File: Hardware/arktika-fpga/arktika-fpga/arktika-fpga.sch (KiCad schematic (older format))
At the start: 0 parts

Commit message: Misc schematic changes. Preliminary layout almost complete
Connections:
- net labels added: D+, D-, GNDPLL0, GNDPLL1
- wire segments 19 -> 25
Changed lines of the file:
@@
 F11 "VCC5V" I R 3850 3900 50
 F12 "GND" I L 2550 4050 50
+F13 "GNDPLL0" I L 2550 3950 50
+F14 "GNDPLL1" I L 2550 3850 50
 $EndSheet
 $Sheet
@@
 F10 "VBUS" I L 4350 3900 50
 F11 "GND" I R 5600 4050 50
+F12 "GNDPLL0" I R 5600 3950 50
+F13 "GNDPLL1" I R 5600 3850 50
 $EndSheet
 $Sheet
@@
 F2 "VCC3V3" I L 6300 3200 50
 F3 "VCC5V" I L 6300 3300 50
-F4 "PUSH_BTNS" I R 7550 3200 50
-F5 "SWITCHES" I R 7550 3300 50
-F6 "LEDS" I R 7550 3400 50
-F7 "ADC" I R 7550 3500 50
-F8 "UART" I R 7550 3600 50
-F9 "Vin" I L 6300 3400 50
-F10 "Buzzer" I R 7550 3700 50
-F11 "GND" I L 6300 4050 50
+F4 "Vin" I L 6300 3400 50
+F5 "Buzzer" I R 7550 3700 50
+F6 "GND" I L 6300 4050 50
+F7 "D+" I L 6300 3550 50
+F8 "D-" I L 6300 3650 50
+F9 "PSH[0..3]" I R 7550 3200 50
+F10 "SW[0..7]" I R 7550 3300 50
+F11 "LED[0..7]" I R 7550 3400 50
 $EndSheet
 $Sheet
@@
 F0 "FPGA_PERIPHS" 50
 F1 "FPGA_PERIPHS.sch" 50
-F2 "PUSH_BTNS" I L 7950 3200 50
-F3 "SWITCHES" I L 7950 3300 50
-F4 "LEDS" I L 7950 3400 50
-F5 "ADC" I L 7950 3500 50
-F6 "UART" I L 7950 3600 50
-F7 "VCC3V3" I R 9250 3200 50
-F8 "Buzzer" I L 7950 3700 50
-F9 "GND" I R 9250 4050 50
+F2 "VCC3V3" I R 9250 3200 50
+F3 "Buzzer" I L 7950 3700 50
+F4 "GND" I R 9250 4050 50
+F5 "PSH[0..3]" I L 7950 3200 50
+F6 "SW[0..7]" I L 7950 3300 50
+F7 "LED[0..7]" I L 7950 3400 50
 $EndSheet
-Wire Bus Line
-	7550 3200 7950 3200
-Wire Bus Line
-	7550 3300 7950 3300
-Wire Bus Line
-	7550 3400 7950 3400
-Wire Bus Line
-	7550 3500 7950 3500
-Wire Bus Line
-	7550 3600 7950 3600
 Wire Wire Line
 	3850 3200 4350 3200
@@
 	2250 4050 2550 4050
 $Comp
-L power:GND #PWR0101
+L arktika-fpga-rescue:GND-power #PWR0101
 U 1 1 5F2E4558
 P 2250 4050
@@
 	5600 4050 5950 4050
 $Comp
-L power:GND #PWR0102
+L arktika-fpga-rescue:GND-power #PWR0102
 U 1 1 5F2E4A9A
 P 5950 4050
@@
 	9550 4050 9250 4050
 $Comp
-L power:GND #PWR0103
+L arktika-fpga-rescue:GND-power #PWR0103
 U 1 1 5F2E5C47
 P 9550 4050
@@
 	1    0    0    -1
 $EndComp
+Text Label 4050 3700 0    50   ~ 0
+D+
+Text Label 4050 3800 0    50   ~ 0
+D-
+Text Label 6100 3550 0    50   ~ 0
+D+
+Text Label 6100 3650 0    50   ~ 0
+D-
+Wire Wire Line
+	5900 3550 6300 3550
+Wire Wire Line
+	5900 3650 6300 3650
+Text Label 6050 3850 2    50   ~ 0
+GNDPLL0
+Text Label 6050 3950 2    50   ~ 0
+GNDPLL1
+Text Label 2150 3850 0    50   ~ 0
+GNDPLL0
+Text Label 2150 3950 0    50   ~ 0
+GNDPLL1
+Wire Wire Line
+	2150 3850 2550 3850
+Wire Wire Line
+	2550 3950 2150 3950
+Wire Wire Line
+	5600 3850 6050 3850
+Wire Wire Line
+	6050 3950 5600 3950
+Wire Bus Line
+	7550 3400 7950 3400
+Wire Bus Line
+	7550 3200 7950 3200
+Wire Bus Line
+	7950 3300 7550 3300
 $EndSCHEMATC

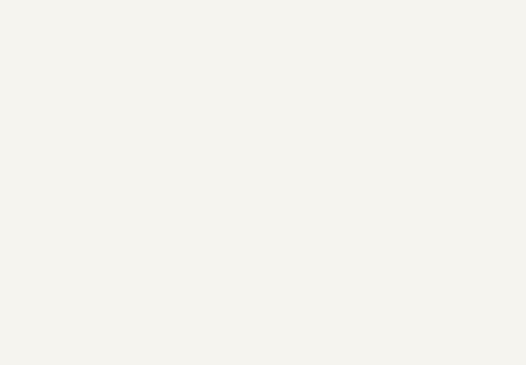
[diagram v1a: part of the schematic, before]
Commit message: Added silkscreen art and added media folder with the same art
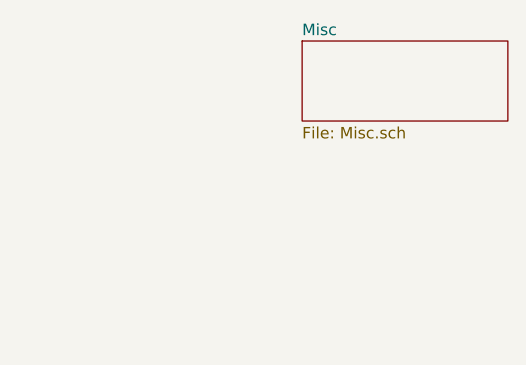
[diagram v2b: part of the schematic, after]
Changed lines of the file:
@@
 $Descr A4 11693 8268
 encoding utf-8
-Sheet 1 5
+Sheet 1 6
 Title "Arktika FPGA"
 Date "2020-07-30"
@@
 Wire Bus Line
 	7950 3300 7550 3300
+$Sheet
+S 9600 1300 900  350
+U 5F28BC74
+F0 "Misc" 50
+F1 "Misc.sch" 50
+$EndSheet
 $EndSCHEMATC
